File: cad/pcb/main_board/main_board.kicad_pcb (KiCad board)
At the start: 2 copper layers, 120 x 100 mm, 72 parts, among them J1 USB_B_Micro, SW1 SW_DIP_x02, SW2 SW_DIP_x01, U1 STM32F401R_B-C_Tx, U2 TLV75533PDRVR

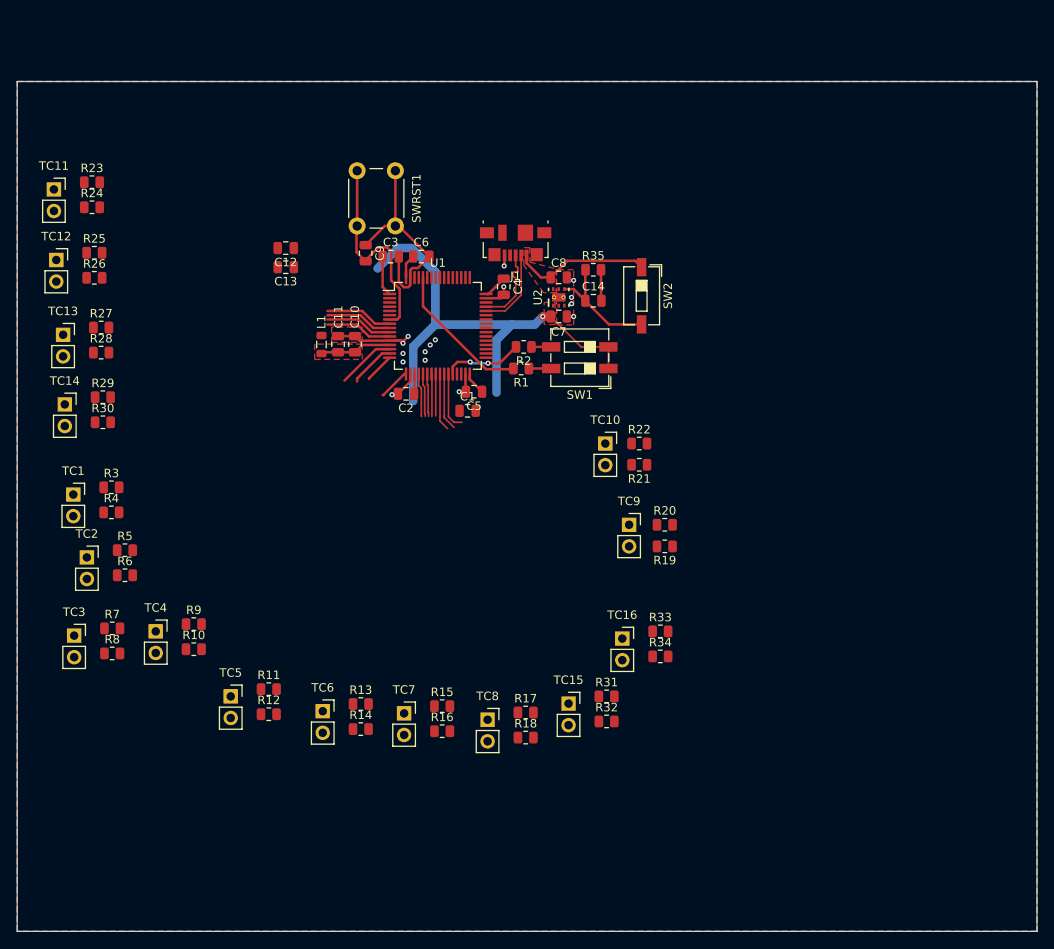
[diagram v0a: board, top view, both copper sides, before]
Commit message: Remove rounded version
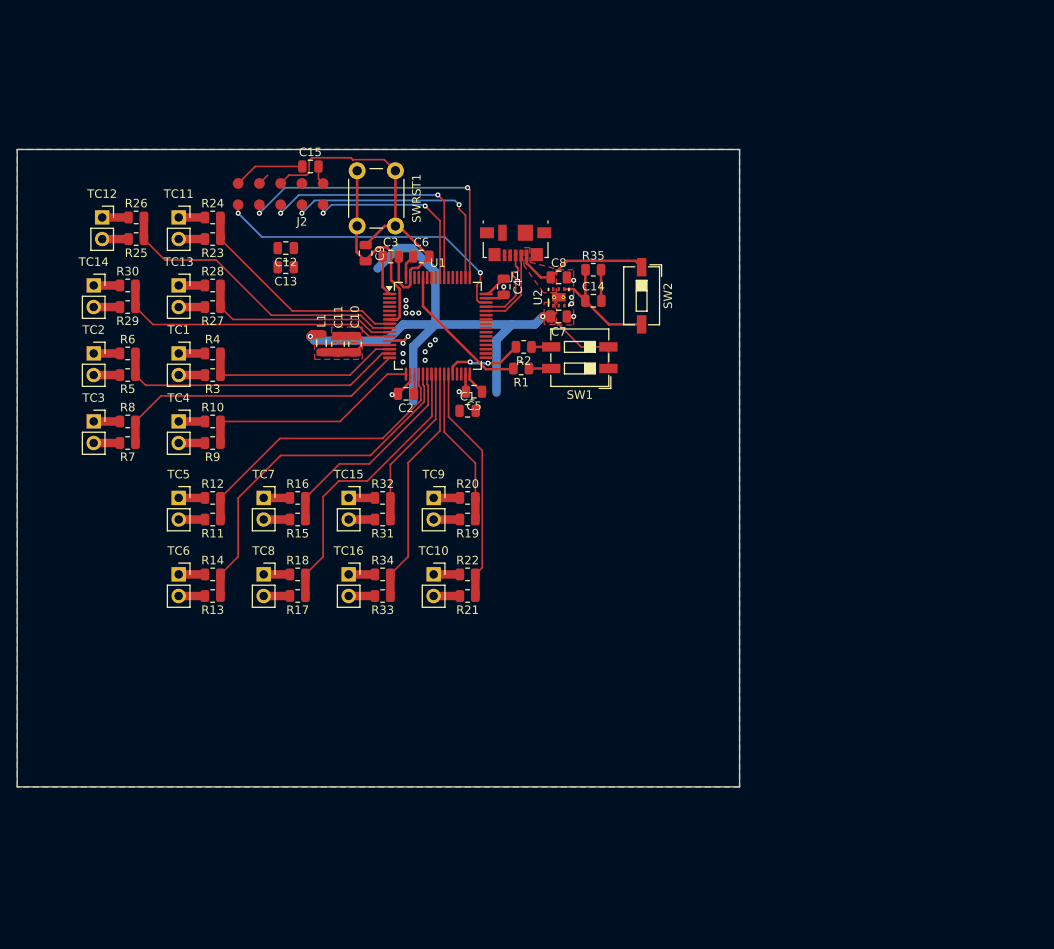
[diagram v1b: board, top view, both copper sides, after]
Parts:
- added C15: C, Capacitor_SMD:C_0805_2012Metric, F.Cu at (94.5, 34.0)
- added J2: Conn_ARM_JTAG_SWD_10, local:POGO_JTAG_SWD, F.Cu at (93.5, 41.0)
- moved R32 37.2 mm to (103.0, 73.0)
- moved TC15 35.4 mm to (99.0, 73.0)
- moved R34 34.1 mm to (103.0, 82.0)
- moved R31 33.6 mm to (103.0, 75.5), turned to 180 degrees
- moved TC16 33.1 mm to (99.0, 82.0)
- moved R18 33.0 mm to (93.0, 82.0)
- moved R33 32.9 mm to (103.0, 84.5), turned to 180 degrees
- moved R16 32.3 mm to (93.0, 73.0)
- moved TC8 31.4 mm to (89.0, 82.0)
- moved TC7 30.3 mm to (89.0, 73.0)
- moved R17 30.1 mm to (93.0, 84.5), turned to 180 degrees
- moved R15 27.8 mm to (93.0, 75.5), turned to 180 degrees
- moved R8 27.4 mm to (73.0, 64.0)
- moved R10 26.9 mm to (83.0, 64.0)
- moved R12 26.3 mm to (83.0, 73.0)
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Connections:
- U1 pad 12: VSS -> VSSA
- U1 pad 46: unconnected-(U1-PA13-Pad46) -> Net-(J2-SWDIO/TMS)
- U1 pad 49: unconnected-(U1-PA14-Pad49) -> Net-(J2-SWCLK/TCK)
- U1 pad 50: unconnected-(U1-PA15-Pad50) -> Net-(J2-NC/TDI)
- U1 pad 55: unconnected-(U1-PB3-Pad55) -> Net-(J2-SWO/TDO)
- U1 pad 56: unconnected-(U1-PB4-Pad56) -> Net-(J2-~{RESET})
- U2 pad 2: VSS -> unconnected-(U2-NC-Pad2)
- U2 pad 5: VSS -> unconnected-(U2-NC-Pad5)
- U2 pad V: VSS -> (no net)
- U2 pad VSS: VSS -> (no net)
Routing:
- net VSSA: track 0.00 -> 51.9 mm
- net Net-(J2-SWCLK/TCK): track 0.00 -> 37.4 mm, vias 0 -> 2
- net /MCU/ADC_IN5: track 5.08 -> 42.3 mm
- net Net-(J2-SWDIO/TMS): track 0.00 -> 37.0 mm, vias 0 -> 2
- net /MCU/ADC_IN2: track 3.50 -> 35.6 mm
- net Net-(J2-SWO/TDO): track 0.00 -> 30.4 mm, vias 0 -> 2
- net /MCU/ADC_IN7: track 5.00 -> 34.3 mm
- net Net-(J2-NC/TDI): track 0.00 -> 29.2 mm, vias 0 -> 2
- net /MCU/ADC_IN1: track 5.40 -> 34.5 mm
- net /MCU/ADC_IN4: track 5.12 -> 34.1 mm
- net /MCU/ADC_IN11: track 7.95 -> 35.8 mm
- net VDD: track 74.2 -> 100.6 mm, vias 1 -> 2
- net /MCU/ADC_IN13: track 7.90 -> 33.9 mm
- net /MCU/ADC_IN3: track 3.78 -> 26.7 mm
- net Net-(J2-~{RESET}): track 0.00 -> 22.6 mm, vias 0 -> 2
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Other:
- board size 120 x 100 mm -> 85 x 75 mm

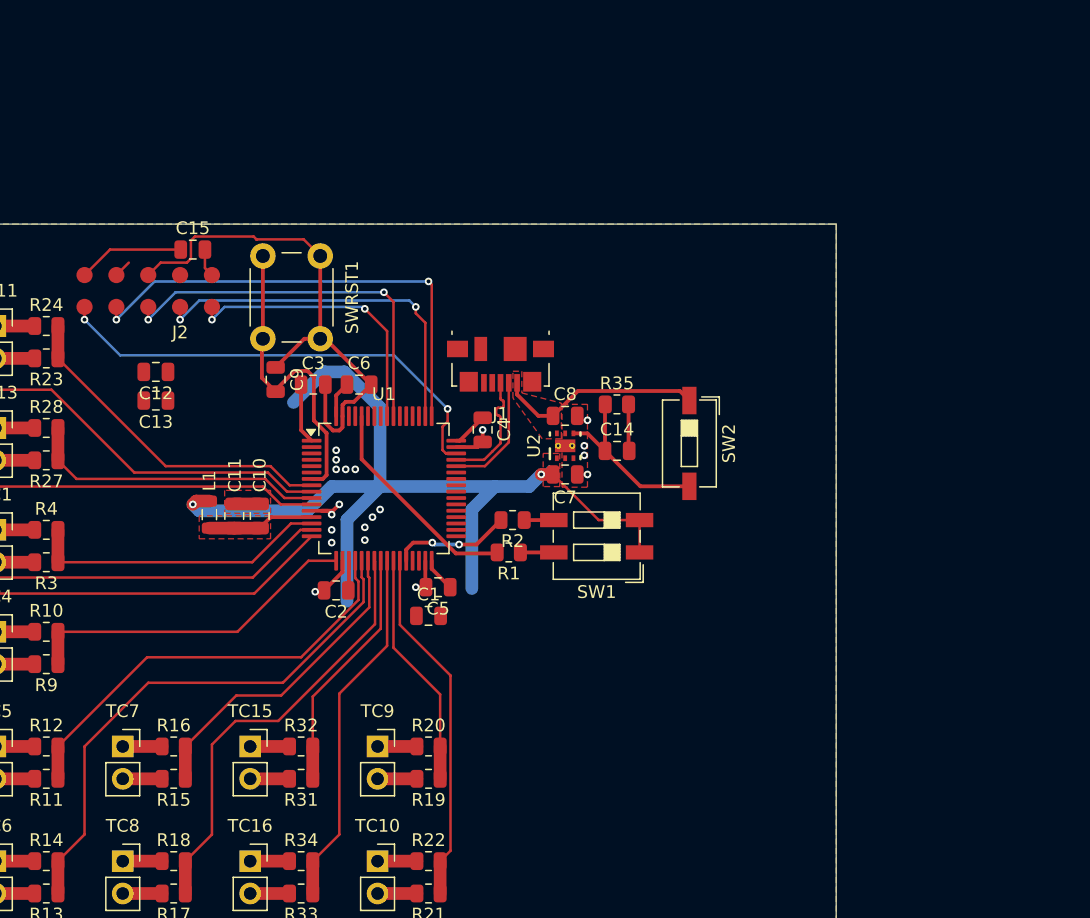
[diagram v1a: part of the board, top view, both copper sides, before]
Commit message: Redo Power And JTAG layout
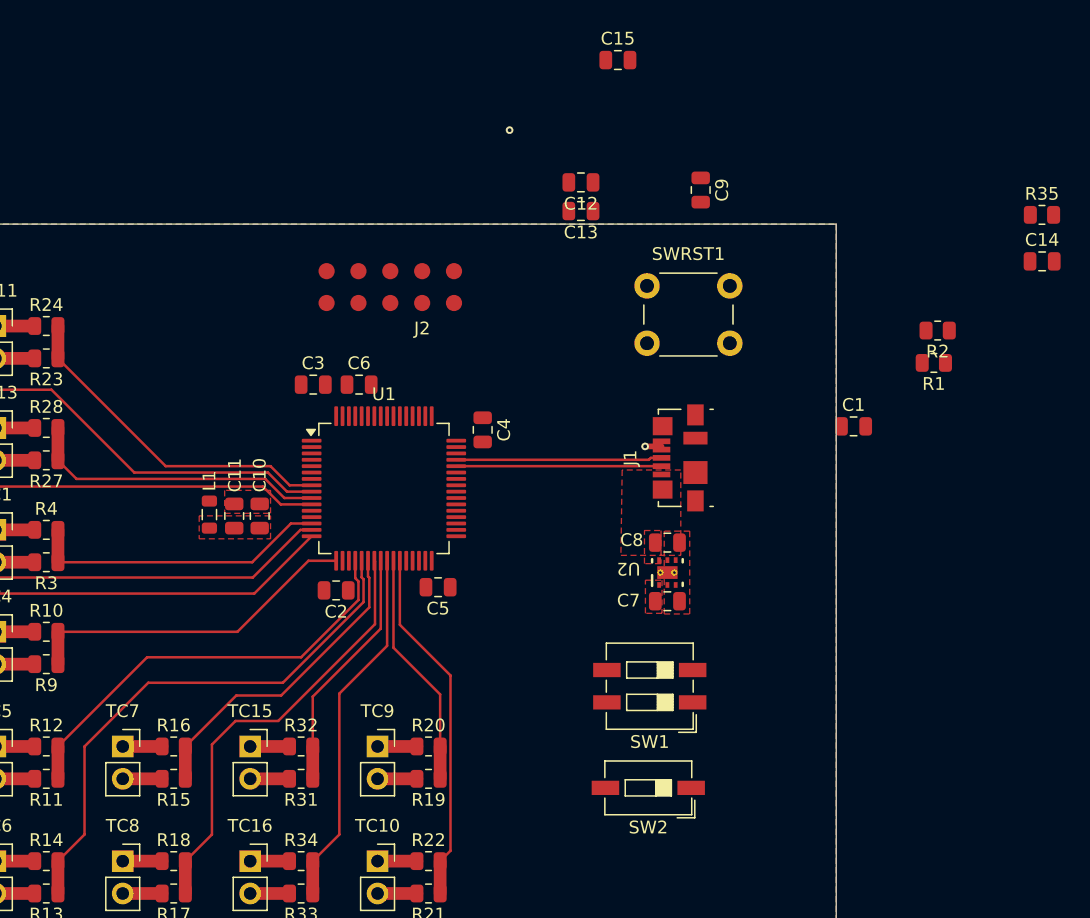
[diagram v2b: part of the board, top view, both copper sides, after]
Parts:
- moved SWRST1 36.7 mm to (136.7, 41.4), turned to 180 degrees
- moved C9 36.5 mm to (134.4, 29.3)
- moved C1 36.5 mm to (146.4, 47.9)
- moved C12 36.5 mm to (125.0, 28.7)
- moved C13 36.5 mm to (125.0, 31.0)
- moved R2 36.5 mm to (153.0, 40.4)
- moved R35 36.5 mm to (161.2, 31.3)
- moved C14 36.5 mm to (161.2, 34.9)
- moved C15 36.5 mm to (127.9, 19.1)
- moved R1 36.5 mm to (152.7, 42.9)
- moved SW2 27.2 mm to (130.2, 76.2), turned to 180 degrees
- moved J2 19.0 mm to (112.5, 40.7)
- moved J1 15.9 mm to (132.8, 50.4), turned to 90 degrees
- moved C7 12.8 mm to (131.8, 61.6)
- moved C8 12.8 mm to (131.8, 57.0)
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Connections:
- U2 pad V: (no net) -> VSS
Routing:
- net VDD: track 100.6 -> 0.00 mm, vias 2 -> 0
- net VSS: track 58.1 -> 0.00 mm, vias 20 -> 0
- net Net-(J2-SWCLK/TCK): track 37.4 -> 0.00 mm, vias 2 -> 0
- net Net-(J2-SWDIO/TMS): track 37.0 -> 0.00 mm, vias 2 -> 1
- net Net-(J2-SWO/TDO): track 30.4 -> 0.00 mm, vias 2 -> 0
- net Net-(J2-NC/TDI): track 29.2 -> 0.00 mm, vias 2 -> 0
- net Net-(U1-NRST): track 24.5 -> 0.00 mm
- net Net-(J2-~{RESET}): track 22.6 -> 0.00 mm, vias 2 -> 0
- net BOOT0: track 17.1 -> 0.00 mm
- net VBUS: track 16.3 -> 0.00 mm
- net Net-(U2-EN): track 14.5 -> 0.00 mm
- net BOOT1: track 9.40 -> 0.00 mm, vias 2 -> 0
- net VDDA: track 8.44 -> 0.00 mm
- net /MCU/USB_D+: track 9.53 -> 16.2 mm
- net /MCU/USB_D-: track 9.57 -> 16.1 mm
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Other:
- board text removed: "This is not good, the ADC IN get the noisiest parts Of the pcb"

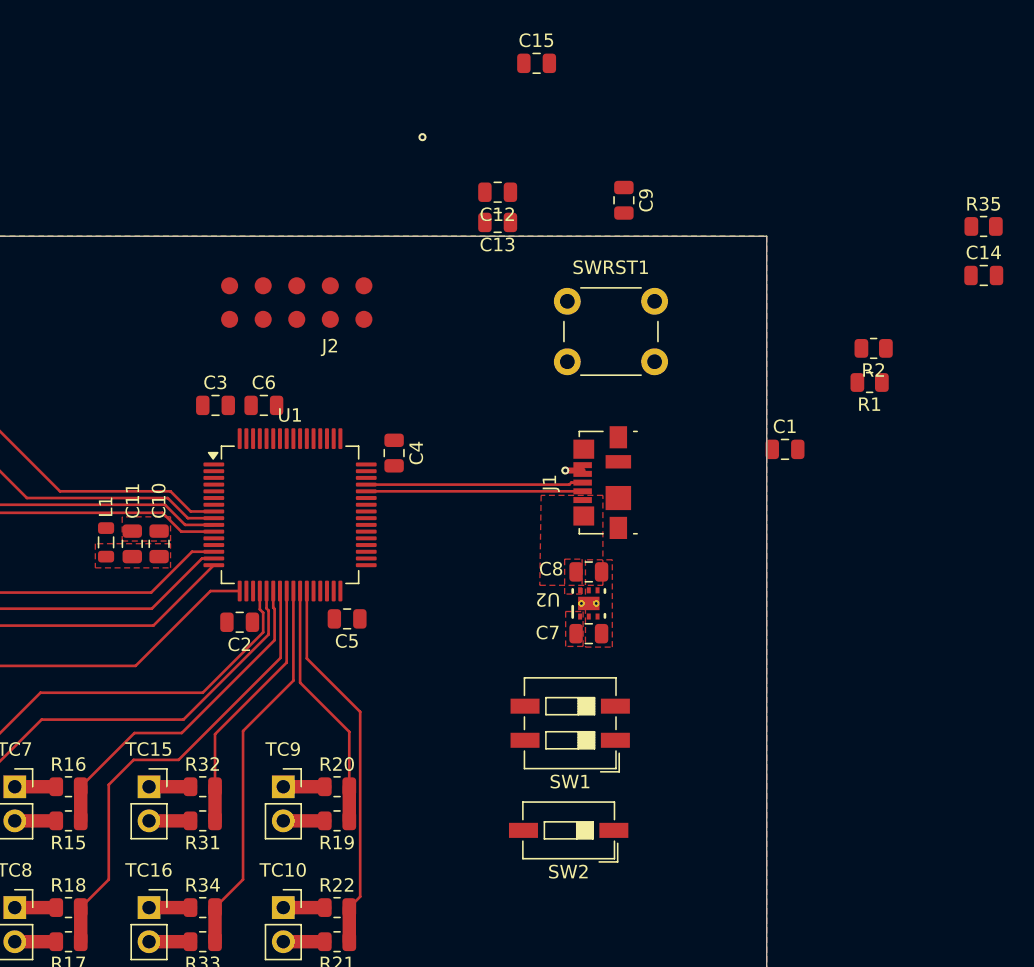
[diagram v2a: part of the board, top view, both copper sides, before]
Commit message: More bunching together, some jtag, voltage regulator layout
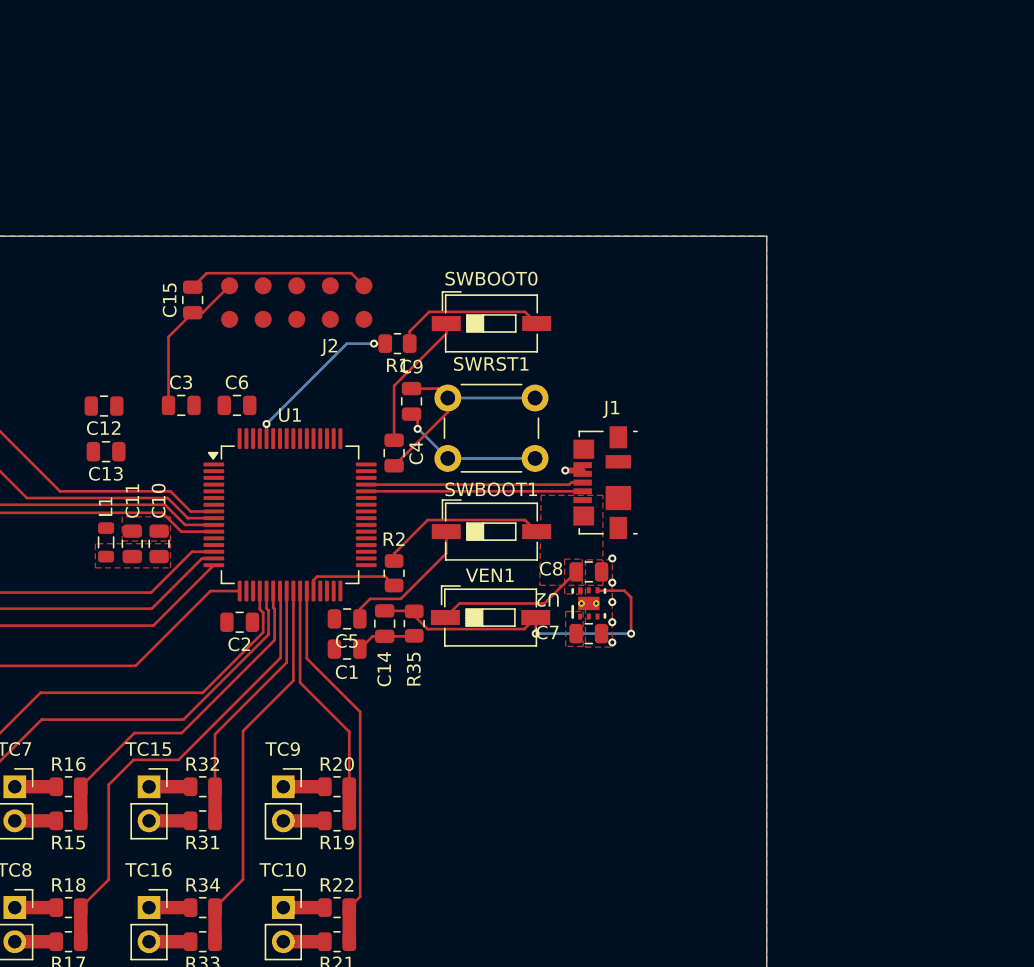
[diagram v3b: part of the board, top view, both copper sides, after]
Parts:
- removed SW1: SW_DIP_x02, Button_Switch_SMD:SW_DIP_SPSTx02_Slide_6.7x6.64mm_W6.73mm_P2.54mm_LowProfile_JPin
- removed SW2: SW_DIP_x01, Button_Switch_SMD:SW_DIP_SPSTx01_Slide_6.7x4.1mm_W6.73mm_P2.54mm_LowProfile_JPin
- added SWBOOT0: SW_DIP_x01, Button_Switch_SMD:SW_DIP_SPSTx01_Slide_6.7x4.1mm_W6.73mm_P2.54mm_LowProfile_JPin, F.Cu at (124.5, 38.5)
- added SWBOOT1: SW_DIP_x01, Button_Switch_SMD:SW_DIP_SPSTx01_Slide_6.7x4.1mm_W6.73mm_P2.54mm_LowProfile_JPin, F.Cu at (124.5, 54.0)
- added VEN1: SW_DIP_x01, Button_Switch_SMD:SW_DIP_SPSTx01_Slide_6.7x4.1mm_W6.73mm_P2.54mm_LowProfile_JPin, F.Cu at (124.4, 60.4)
- moved R35 51.7 mm to (118.8, 60.9), turned to -90 degrees
- moved C14 51.6 mm to (116.5, 60.9), turned to -90 degrees
- moved R2 39.4 mm to (117.2, 57.1), turned to -90 degrees
- moved C1 35.8 mm to (113.8, 62.8)
- moved R1 35.3 mm to (117.5, 40.0)
- moved C13 33.8 mm to (95.8, 48.0)
- moved C12 33.4 mm to (95.7, 44.6)
- moved C15 31.1 mm to (102.2, 36.8), turned to 90 degrees
- moved C9 21.8 mm to (118.5, 44.3)
- moved SWRST1 11.4 mm to (127.8, 48.5)
- moved C3 2.55 mm to (101.4, 44.6)
- moved C6 2.00 mm to (105.5, 44.6)
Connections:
- U2 pad V: VSS -> (no net)
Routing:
- net VDD: track 0.00 -> 32.1 mm
- net Net-(U2-EN): track 0.00 -> 26.1 mm, vias 0 -> 2
- net VSS: track 0.00 -> 20.7 mm, vias 0 -> 5
- net Net-(J2-GNDDetect): track 0.00 -> 13.6 mm
- net Net-(R2-Pad1): track 0.00 -> 12.6 mm
- net BOOT0: track 0.00 -> 12.4 mm, vias 0 -> 2
- net Net-(R1-Pad1): track 0.00 -> 11.3 mm
- net VBUS: track 0.00 -> 11.1 mm
- net Net-(U1-NRST): track 0.00 -> 10.9 mm, vias 0 -> 1
- net BOOT1: track 0.00 -> 7.19 mm
- net Net-(J2-SWDIO/TMS): vias 1 -> 0

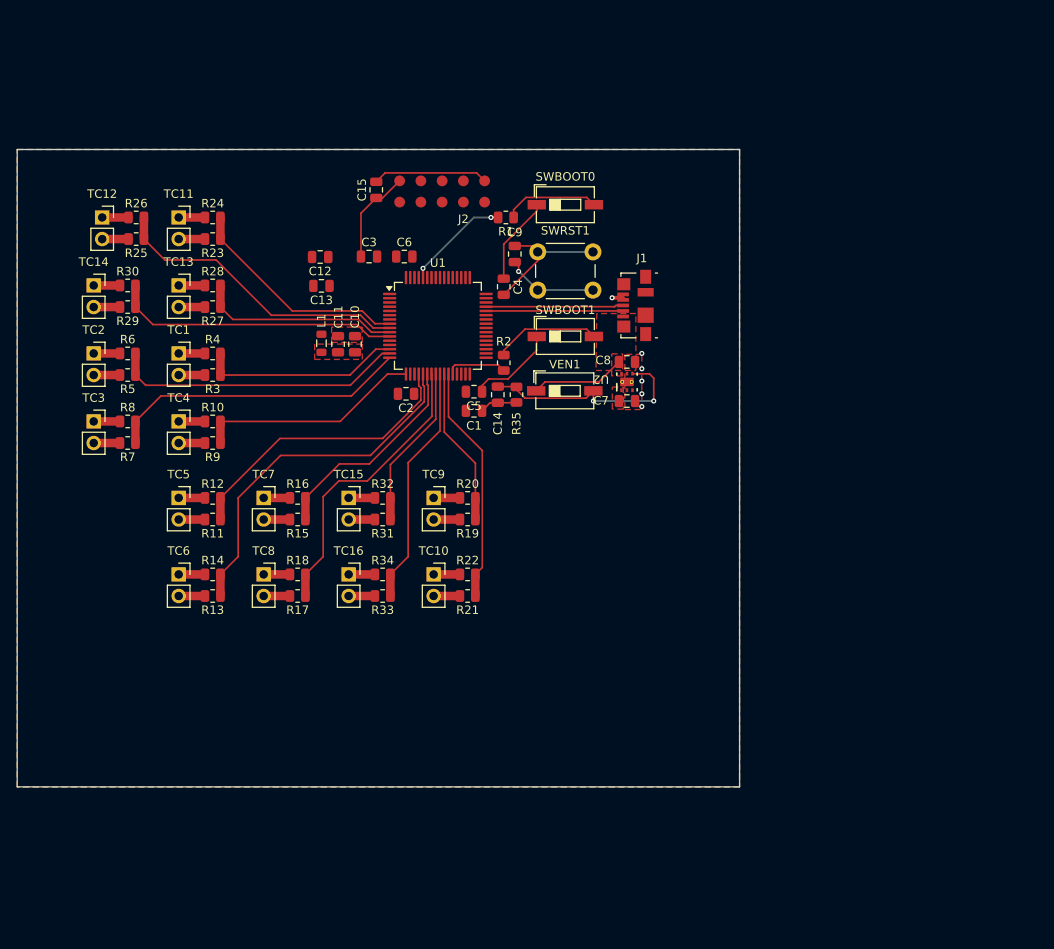
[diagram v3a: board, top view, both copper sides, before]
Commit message: Oscillator Selection an and Layouting
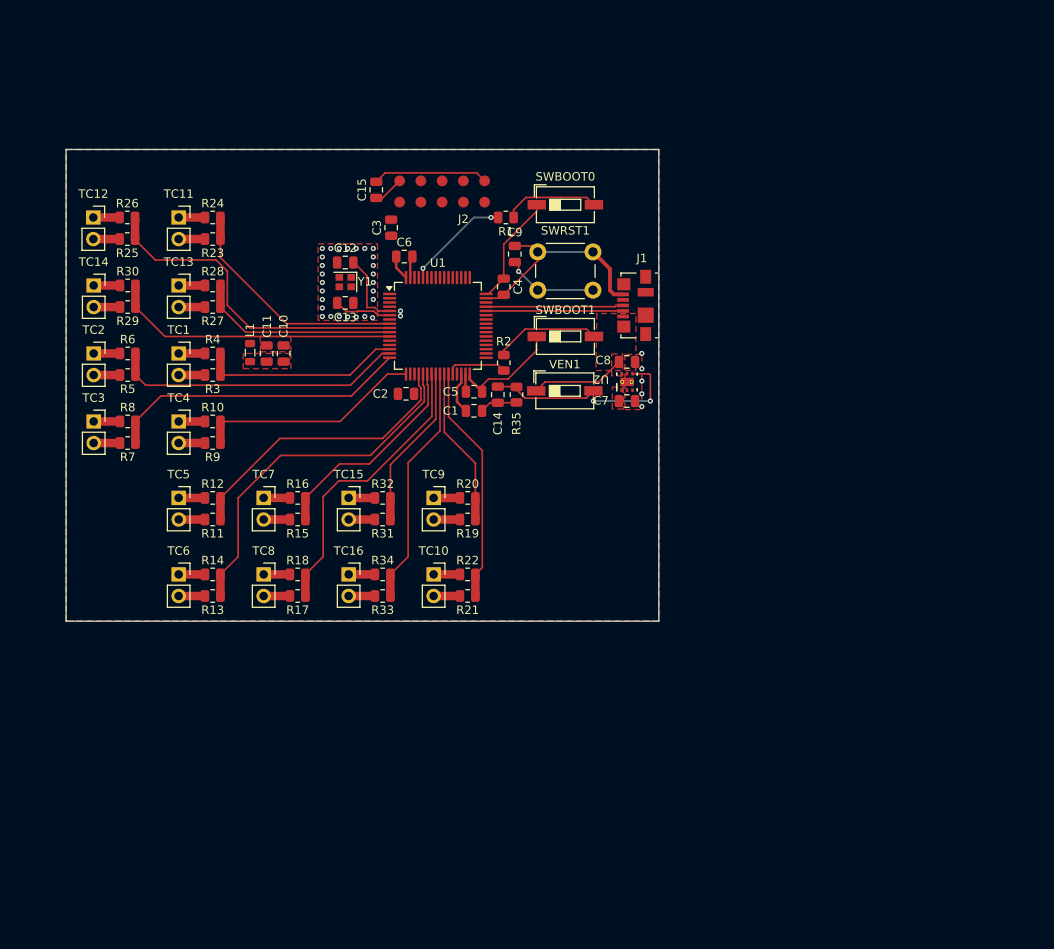
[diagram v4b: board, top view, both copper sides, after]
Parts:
- added Y1: Crystal_GND23, Crystal:Crystal_SMD_2016-4Pin_2.0x1.6mm, F.Cu at (98.6, 47.6)
- moved C10 8.47 mm to (91.3, 56.0)
- moved C11 8.47 mm to (89.3, 56.0)
- moved L1 8.47 mm to (87.4, 55.9)
- moved C3 4.28 mm to (104.0, 41.2), turned to 90 degrees
- moved C13 3.44 mm to (98.6, 50.0), turned to 0 degrees
- moved C12 3.02 mm to (98.6, 45.3)
- moved R25 1.04 mm to (73.0, 42.5)
- moved R26 1.04 mm to (73.0, 40.0)
- moved TC12 1.04 mm to (69.0, 40.0)
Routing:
- net VSS: track 20.7 -> 35.5 mm, vias 5 -> 34
- net Net-(U1-PH0): track 0.00 -> 9.21 mm
- net Net-(U1-PH1): track 0.00 -> 6.84 mm
- net Net-(U1-VCAP1): track 0.00 -> 4.97 mm
- net /MCU/ADC_IN11: track 35.8 -> 39.2 mm
- net /MCU/USB_ID: track 1.29 -> 0.00 mm, vias 1 -> 0
- net /MCU/ADC_IN10: track 26.6 -> 27.9 mm
- net VDD: track 32.1 -> 32.9 mm
- net Net-(U2-EN): track 26.1 -> 25.5 mm
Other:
- board size 85 x 75 mm -> 69.8 x 55.5 mm
